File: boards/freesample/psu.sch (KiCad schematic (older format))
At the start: 162 parts, among them U26 MCP1755ST-5002E/MC, U27 LM27761, U28 ADP1763Z-1.0, U29 ADP1763Z-1.0, U30 OKL-T/3-W12P-C, U31 ADP1741, U32 OKL-T/3-W12P-C, U33 ADP1741, U34 ADP1741, U35 OKL-T/3-W12P-C, U36 OKL-T/3-W12P-C, U37 LM27761, U38 OKL-T/3-W12P-C, U39 LM27761, U42 ADP1741, U43 ADP1741

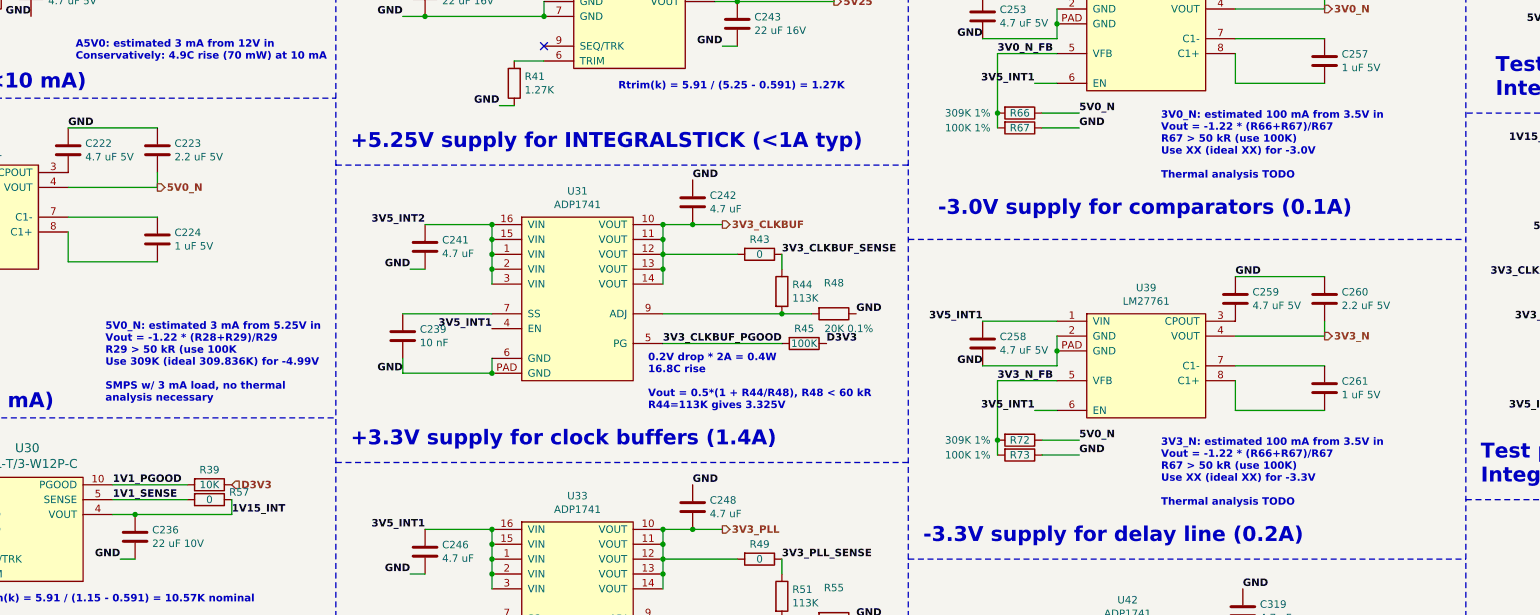
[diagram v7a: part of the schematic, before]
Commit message: Finished schematic review. Added a bunch more test points. Need to make a few footprints then ready for layout!
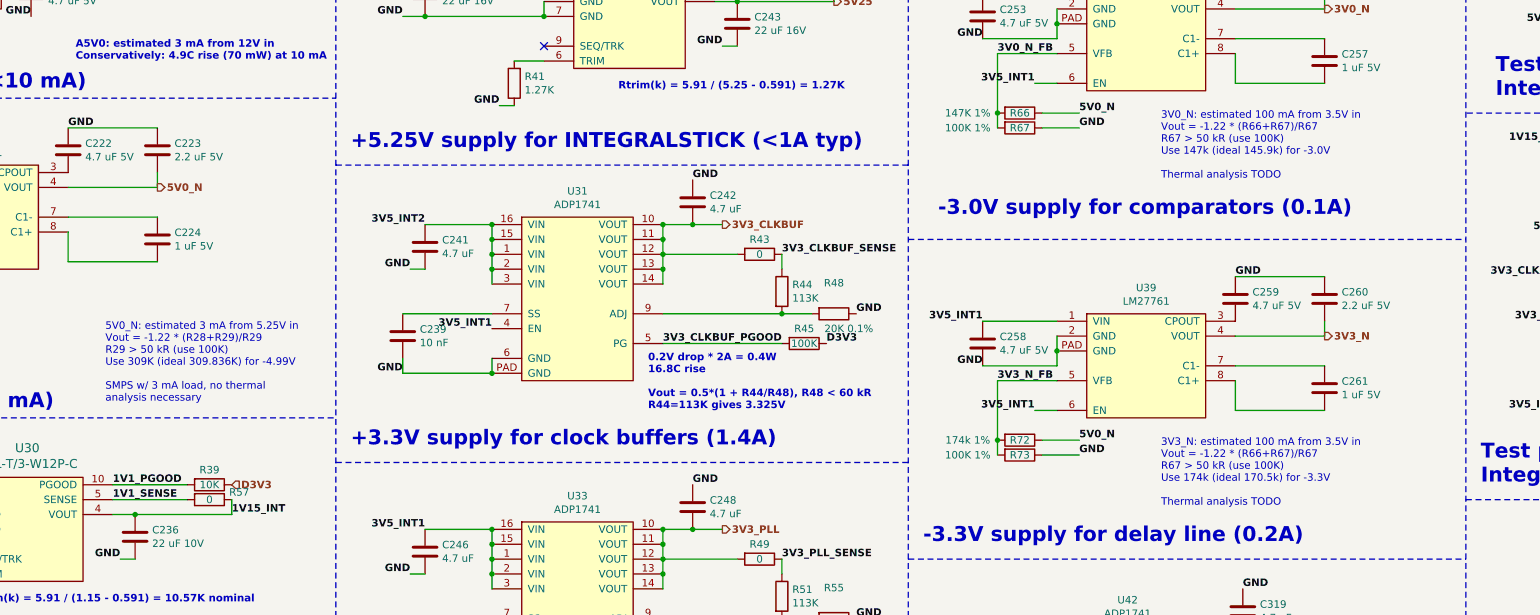
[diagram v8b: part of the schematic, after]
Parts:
- R66: value 309K 1% -> 147K 1%
- R72: value 309K 1% -> 174k 1%
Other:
- note added: "3V0_N: estimated 100 mA from 3.5V in\nVout = -1.22 * (R66+R67)/R67\nR67 > 50 kR (use 100K)\nUse 147k (ideal 145.9k) for -3.0V\n\nThermal analysis TODO"
- note added: "3V3_N: estimated 100 mA from 3.5V in\nVout = -1.22 * (R66+R67)/R67\nR67 > 50 kR (use 100K)\nUse 174k (ideal 170.5k) for -3.3V\n\nThermal analysis TODO"
- note added: "5V0_N: estimated 3 mA from 5.25V in\nVout = -1.22 * (R28+R29)/R29\nR29 > 50 kR (use 100K)\nUse 309K (ideal 309.836K) for -4.99V\n\nSMPS w/ 3 mA load, no thermal\nanalysis necessary"
- note removed: "3V0_N: estimated 100 mA from 3.5V in\nVout = -1.22 * (R66+R67)/R67\nR67 > 50 kR (use 100K)\nUse XX (ideal XX) for -3.0V\n\nThermal analysis TODO"
- note removed: "3V3_N: estimated 100 mA from 3.5V in\nVout = -1.22 * (R66+R67)/R67\nR67 > 50 kR (use 100K)\nUse XX (ideal XX) for -3.3V\n\nThermal analysis TODO"
- note removed: "5V0_N: estimated 3 mA from 5.25V in\nVout = -1.22 * (R28+R29)/R29\nR29 > 50 kR (use 100K\nUse 309K (ideal 309.836K) for -4.99V\n\nSMPS w/ 3 mA load, no thermal\nanalysis necessary"
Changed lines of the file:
@@
 Wire Wire Line
 	1550 3100 1300 3100
-Text Notes 2850 3750 0    50   ~ 6
-5V0_N: estimated 3 mA from 5.25V in\nVout = -1.22 * (R28+R29)/R29\nR29 > 50 kR (use 100K\nUse 309K (ideal 309.836K) for -4.99V\n\nSMPS w/ 3 mA load, no thermal\nanalysis necessary
+Text Notes 2850 3750 0    50   ~ 0
+5V0_N: estimated 3 mA from 5.25V in\nVout = -1.22 * (R28+R29)/R29\nR29 > 50 kR (use 100K)\nUse 309K (ideal 309.836K) for -4.99V\n\nSMPS w/ 3 mA load, no thermal\nanalysis necessary
 Text Notes 1200 9700 0    50   ~ 6
 Vout = 3.0 * (Radj * 50 uA)\nRadj = 1V/(150 uA) = 6.667 kR\nUse 6.65K for 0.9975V\n\nConnect two in parallel to spread out heat generation\n0.15V * 3A = 0.45W total, estimate 0.3W worst case per chip\nAssuming 1cm^2 plane for heatsinking, 30.8C rise.\nBigger planes will improve this\nTypical SERDES power is << 3A which will also help,\nespecially if we power down the unused channel
@@
 P 9000 1800
 F 0 "R66" V 9000 1800 50  0000 C CNN
-F 1 "309K 1%" V 9000 1450 50  0000 C CNN
+F 1 "147K 1%" V 9000 1450 50  0000 C CNN
 F 2 "azonenberg_pcb:EIA_0402_RES_NOSILK" V 8930 1800 50  0001 C CNN
 F 3 "" H 9000 1800 50  0001 C CNN
@@
 Wire Wire Line
 	9400 1900 9150 1900
-Text Notes 9950 2250 0    50   ~ 6
-3V0_N: estimated 100 mA from 3.5V in\nVout = -1.22 * (R66+R67)/R67\nR67 > 50 kR (use 100K)\nUse XX (ideal XX) for -3.0V\n\nThermal analysis TODO
+Text Notes 9950 2250 0    50   ~ 0
+3V0_N: estimated 100 mA from 3.5V in\nVout = -1.22 * (R66+R67)/R67\nR67 > 50 kR (use 100K)\nUse 147k (ideal 145.9k) for -3.0V\n\nThermal analysis TODO
 Text Label 8750 3200 2    50   ~ 6
 3V5_INT1
@@
 P 9000 4000
 F 0 "R72" V 9000 4000 50  0000 C CNN
-F 1 "309K 1%" V 9000 3650 50  0000 C CNN
+F 1 "174k 1%" V 9000 3650 50  0000 C CNN
 F 2 "azonenberg_pcb:EIA_0402_RES_NOSILK" V 8930 4000 50  0001 C CNN
 F 3 "" H 9000 4000 50  0001 C CNN
@@
 Wire Wire Line
 	9400 4100 9150 4100
-Text Notes 9950 4450 0    50   ~ 6
-3V3_N: estimated 100 mA from 3.5V in\nVout = -1.22 * (R66+R67)/R67\nR67 > 50 kR (use 100K)\nUse XX (ideal XX) for -3.3V\n\nThermal analysis TODO
+Text Notes 9950 4450 0    50   ~ 0
+3V3_N: estimated 100 mA from 3.5V in\nVout = -1.22 * (R66+R67)/R67\nR67 > 50 kR (use 100K)\nUse 174k (ideal 170.5k) for -3.3V\n\nThermal analysis TODO
 Wire Notes Line width 20 style solid
 	8250 2650 12000 2650
